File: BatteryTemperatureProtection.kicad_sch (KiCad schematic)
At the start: 5 parts, among them U11 BTS5090-1EJA

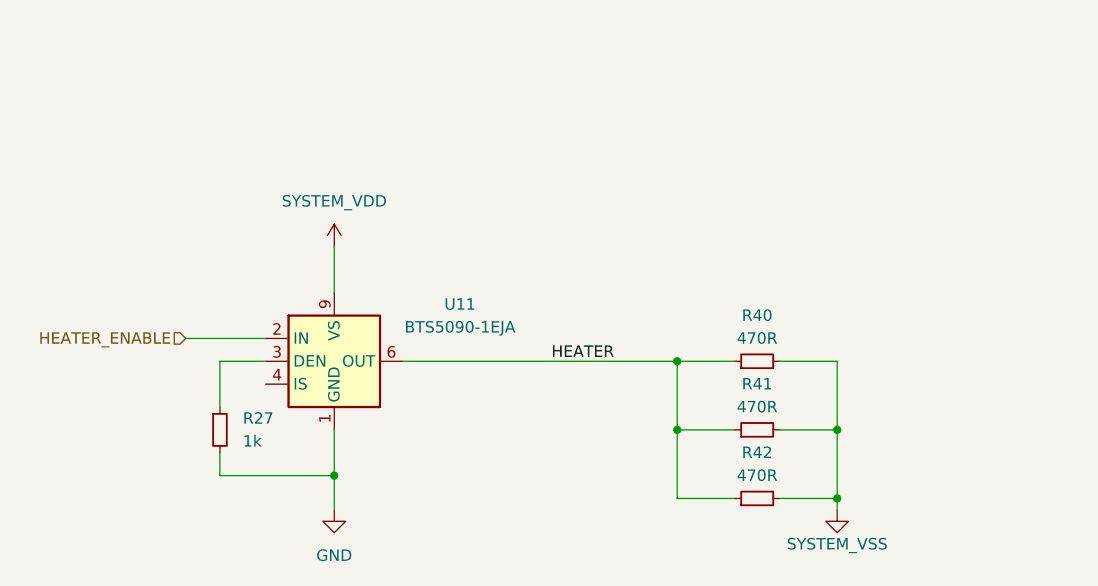
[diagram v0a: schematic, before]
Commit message: Refactored schematics and silkscreen
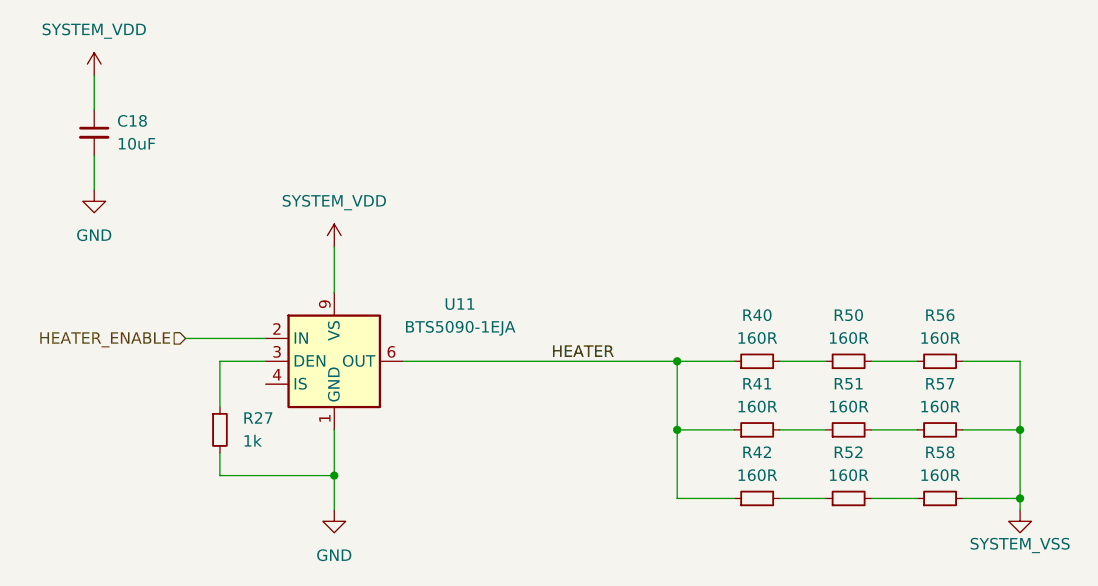
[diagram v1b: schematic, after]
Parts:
- added C18: 10uF, Capacitor_SMD:C_0805_2012Metric, symbol Device:C_Small
- added R50, R51, R52, R56, R57, R58: 160R, Resistor_SMD:R_2010_5025Metric, symbol Device:R_Small
- R27: footprint (none) -> Resistor_SMD:R_0603_1608Metric
- R40, R41, R42: value 470R -> 160R; footprint (none) -> Resistor_SMD:R_2010_5025Metric
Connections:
- net GND: now also C18.2
- net SYSTEM_VDD: now also C18.1
- net SYSTEM_VSS: now also R56.2, R57.2, R58.2; no longer R40.2, R41.2, R42.2
- new net: R51.2, R57.1
- new net: R42.2, R52.1
- new net: R52.2, R58.1
- new net: R40.2, R50.1
- new net: R50.2, R56.1
- new net: R41.2, R51.1
